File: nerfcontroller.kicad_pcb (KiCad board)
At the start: 2 copper layers, 59.7 x 48.3 mm, 40 parts, among them J1 Conn_01x02_Pin, J10 Conn_01x03_Pin, J11 Conn_01x03_Pin, J12 Conn_01x03_Pin, J13 Conn_01x03_Pin, J14 Conn_01x03_Pin, J15 Conn_01x02_Pin, J16 Conn_01x02_Pin, J17 Conn_01x03_Pin, J2 Conn_01x02_Pin, J3 Conn_01x02_Pin, J4 Conn_01x02_Pin, J5 Conn_01x03_Pin, J6 Conn_01x03_Pin, J7 Conn_01x03_Pin, J8 Conn_01x03_Pin, J9 Conn_01x03_Pin, Q1 IRL530, Q2 IRL530, Q3 IRL530, Q4 IRL530, U1 LM7805_TO220

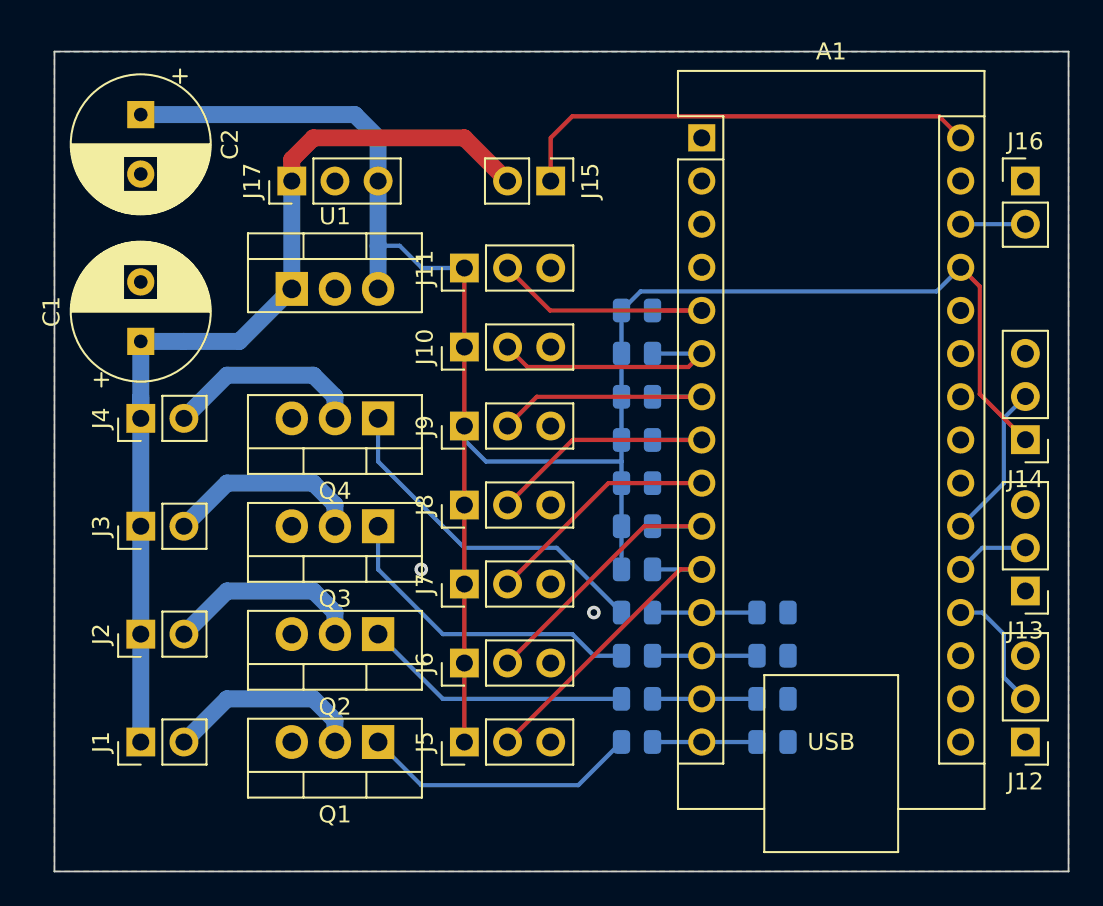
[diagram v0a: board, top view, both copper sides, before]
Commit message: added resistor values for mosfets
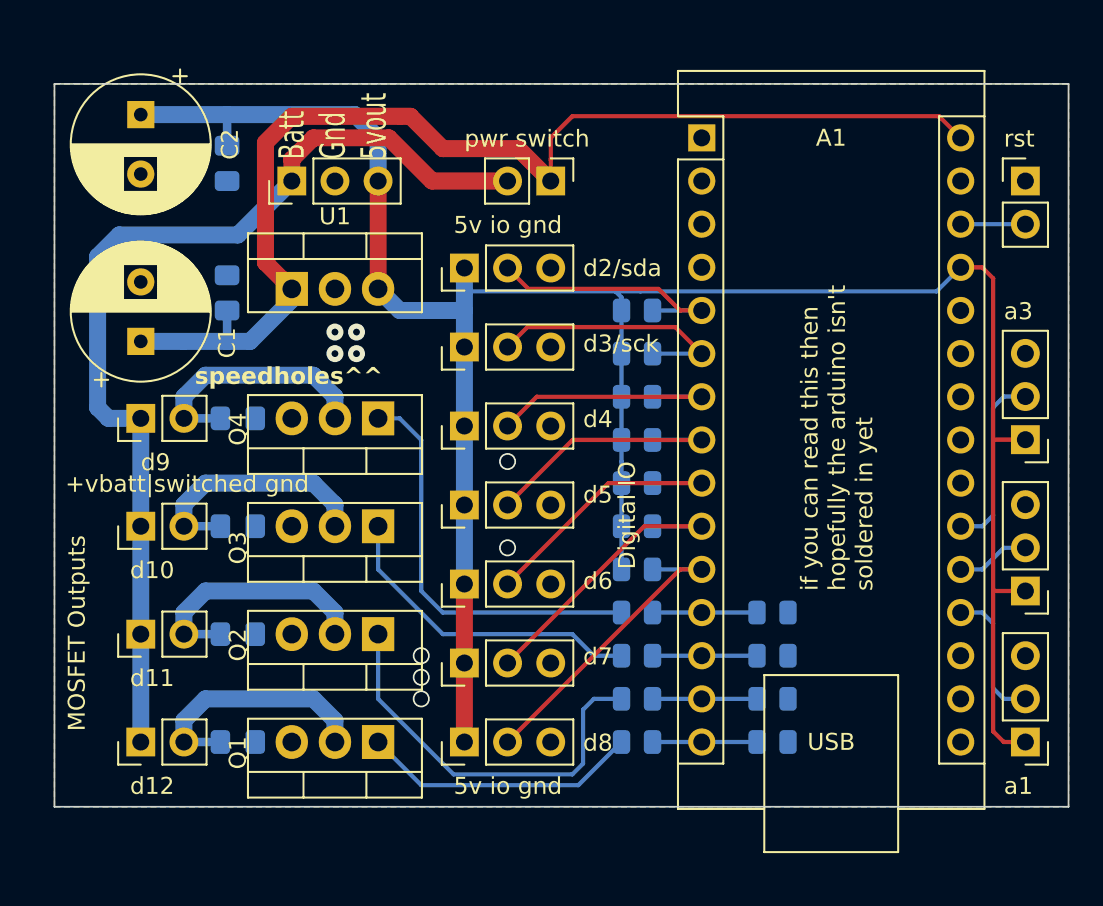
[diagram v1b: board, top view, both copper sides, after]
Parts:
- added C3: C, Capacitor_SMD:C_0805_2012Metric_Pad1.18x1.45mm_HandSolder, B.Cu at (85.1, 105.6)
- added C4: C, Capacitor_SMD:C_0805_2012Metric_Pad1.18x1.45mm_HandSolder, B.Cu at (85.1, 98.0)
- added D1: D, Diode_SMD:D_0805_2012Metric_Pad1.15x1.40mm_HandSolder, B.Cu at (85.7, 113.0)
- added D2: D, Diode_SMD:D_0805_2012Metric_Pad1.15x1.40mm_HandSolder, B.Cu at (85.7, 119.4)
- added D3: D, Diode_SMD:D_0805_2012Metric_Pad1.15x1.40mm_HandSolder, B.Cu at (85.7, 125.7)
- added D4: D, Diode_SMD:D_0805_2012Metric_Pad1.15x1.40mm_HandSolder, B.Cu at (85.7, 132.1)
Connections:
- A1 pad 30: Net-(A1-VIN) -> /12v switched
- C1 pad 1: +12V -> /12v switched
- J15 pad 1: Net-(A1-VIN) -> /12v switched
- U1 pad 1: +12V -> /12v switched
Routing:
- net /12v switched: track 0.00 -> 68.3 mm
- net Net-(A1-VIN): track 27.7 -> 0.00 mm
- net +5V: track 115.5 -> 141.4 mm
- net Net-(Q2-Pad1): track 15.9 -> 23.7 mm
- net Net-(Q4-Pad1): track 20.5 -> 24.3 mm
- net /mosfet1: track 11.7 -> 14.6 mm
- net /mosfet2: track 11.7 -> 14.6 mm
- net /mosfet4: track 11.7 -> 14.6 mm
- net /mosfet3: track 11.7 -> 14.6 mm
- net +12V: track 56.9 -> 59.6 mm
- net /a2: track 9.21 -> 10.7 mm
- net /a0: track 7.40 -> 8.15 mm
- net GND: vias 2 -> 9
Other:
- board size 59.7 x 48.3 mm -> 59.7 x 42.5 mm
- board text added: "+vbatt|switched gnd"
- board text added: "5v io gnd"
- board text added: "Batt Gnd 5vout"
- board text added: "Digital IO"
- board text added: "MOSFET Outputs"
- board text added: "a1"
- board text added: "a3"
- board text added: "d10"
- board text added: "d11"
- board text added: "d12"
- board text added: "d2/sda"
- board text added: "d3/sck"
- board text added: "d4"
- board text added: "d5"
- board text added: "d6"
- board text added: "d7"
- board text added: "d8"
- board text added: "d9"
- board text added: "if you can read this then hopefully the arduino isn't soldered in yet"
- board text added: "pwr switch"
- board text added: "rst"
- board text added: "speedholes^^"
- board text added: "|-optional pullups-|"

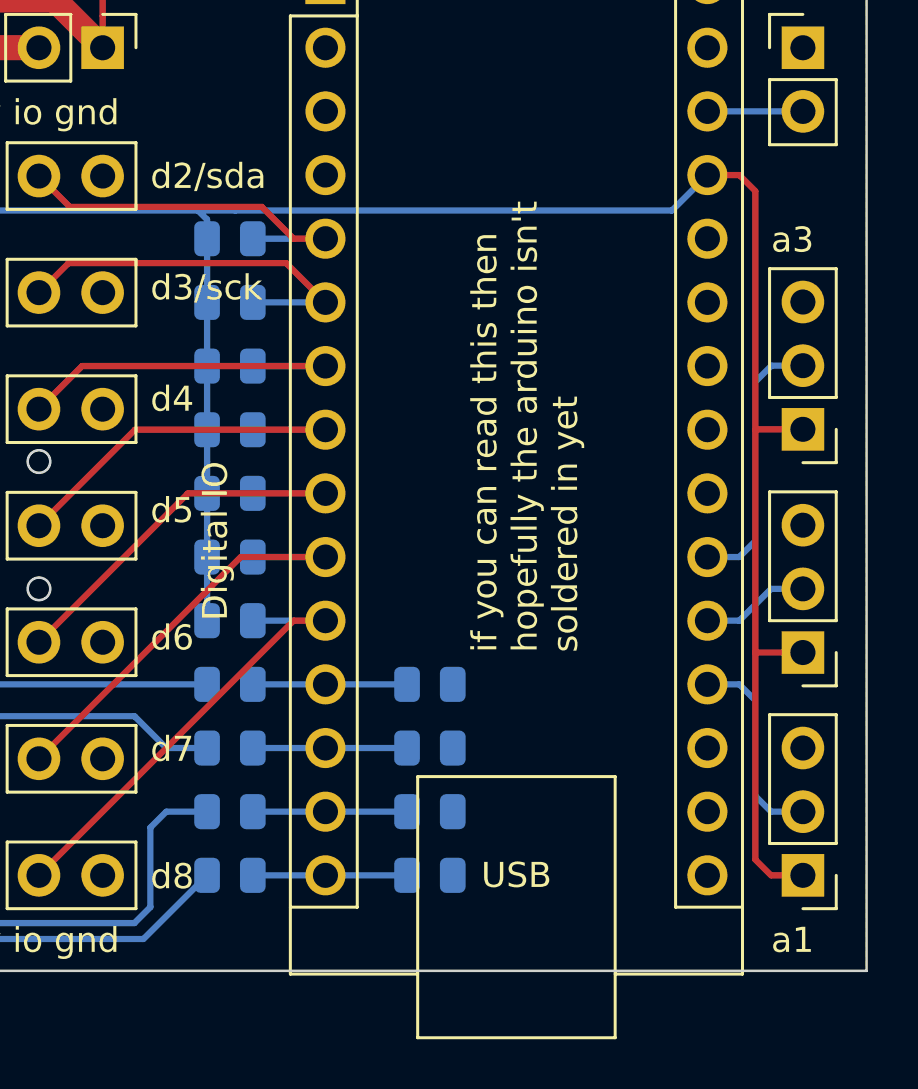
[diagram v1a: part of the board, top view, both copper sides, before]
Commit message: corrected resistor values + silkscreen goofs
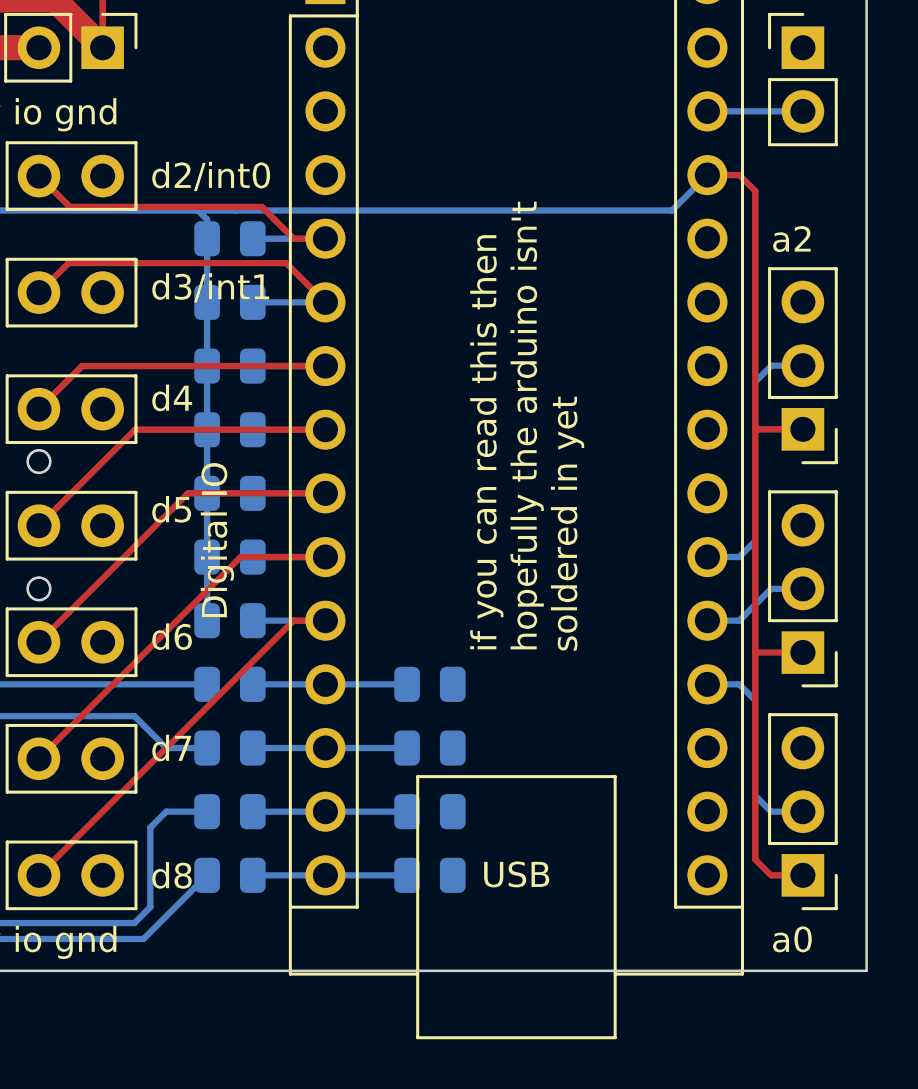
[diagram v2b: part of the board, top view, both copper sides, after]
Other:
- board text added: "a0"
- board text added: "a2"
- board text added: "d2/int0"
- board text added: "d3/int1"
- board text removed: "a1"
- board text removed: "a3"
- board text removed: "d2/sda"
- board text removed: "d3/sck"
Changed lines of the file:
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@@
     (property "ki_keywords" "cap capacitor")
     (attr smd)
-    (fp_text reference "C3" (at 0 1.68 90) (layer "B.SilkS")
+    (fp_text reference "C3" (at -0.027164 -1.677462 90) (layer "B.SilkS")
         (effects (font (size 1 1) (thickness 0.15)) (justify mirror))
     )
@@
     (effects (font (size 1.5 1) (thickness 0.15)) (justify left bottom))
   )
-  (gr_text "a1" (at 130.81 135.255) (layer "F.SilkS")
+  (gr_text "a0" (at 130.81 135.255) (layer "F.SilkS")
     (effects (font (size 1 1) (thickness 0.15)) (justify left bottom))
   )
@@
     (effects (font (size 1 1) (thickness 0.15)) (justify left bottom))
   )
-  (gr_text "d3/sck" (at 106.045 109.22) (layer "F.SilkS")
+  (gr_text "d3/int1" (at 106.045 109.22) (layer "F.SilkS")
     (effects (font (size 1 1) (thickness 0.15)) (justify left bottom))
   )
@@
     (effects (font (size 1 1) (thickness 0.15)) (justify left bottom))
   )
-  (gr_text "a3" (at 130.81 107.315) (layer "F.SilkS")
+  (gr_text "a2" (at 130.81 107.315) (layer "F.SilkS")
     (effects (font (size 1 1) (thickness 0.15)) (justify left bottom))
   )
@@
     (effects (font (size 1 1) (thickness 0.15)) (justify left bottom))
   )
-  (gr_text "d2/sda" (at 106.045 104.775) (layer "F.SilkS")
-    (effects (font (size 1 1) (thickness 0.15)) (justify left bottom))
-  )
+  (gr_text "d2/int0" (at 106.045 104.775) (layer "F.SilkS")
+    (effects (font (size 1 1) (thickness 0.15)) (justify left bottom))
+  )

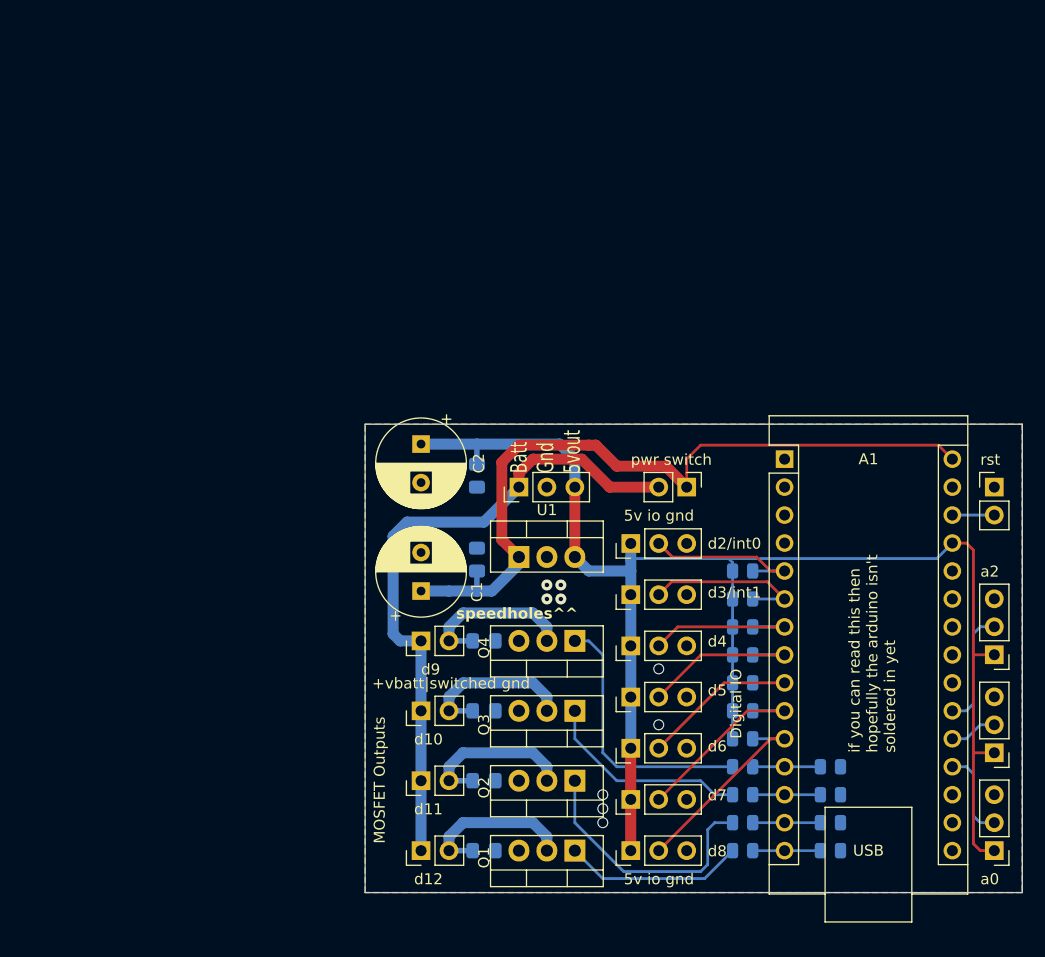
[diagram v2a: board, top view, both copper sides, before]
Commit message: added mosfet drivers and sot23 diodes
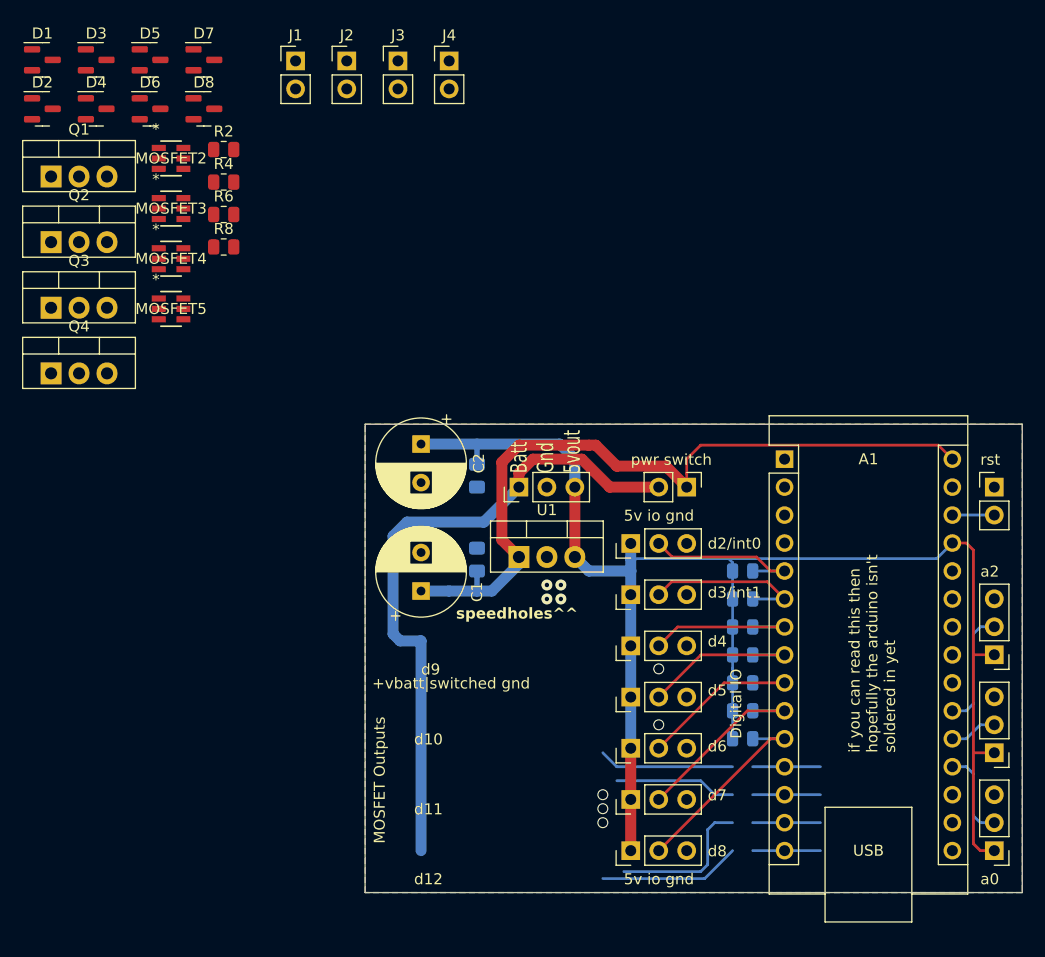
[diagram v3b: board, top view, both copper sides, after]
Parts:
- removed R1, R3, R5, R7: R, Resistor_SMD:R_0805_2012Metric
- added D5: BAV23C, Package_TO_SOT_SMD:SOT-23, F.Cu at (55.4, 60.2)
- added D6: BAV23C, Package_TO_SOT_SMD:SOT-23, F.Cu at (55.4, 64.7)
- added D7: BAV23C, Package_TO_SOT_SMD:SOT-23, F.Cu at (60.3, 60.2)
- added D8: BAV23C, Package_TO_SOT_SMD:SOT-23, F.Cu at (60.3, 64.7)
- added MOSFET2: IRS10752LTRPBF, IRS10752PBF:6L-SOT23, F.Cu at (57.3, 69.2)
- added MOSFET3: IRS10752LTRPBF, IRS10752PBF:6L-SOT23, F.Cu at (57.3, 73.8)
- added MOSFET4: IRS10752LTRPBF, IRS10752PBF:6L-SOT23, F.Cu at (57.3, 78.3)
- added MOSFET5: IRS10752LTRPBF, IRS10752PBF:6L-SOT23, F.Cu at (57.3, 82.9)
- D1, D2, D3, D4: value D -> BAV23C; footprint Diode_SMD:D_0805_2012Metric_Pad1.15x1.40mm_HandSolder -> Package_TO_SOT_SMD:SOT-23; moved to F.Cu
- R2, R4, R6, R8: value R -> 4R7; moved to F.Cu
- moved R2 84.2 mm to (62.1, 68.4)
- moved R4 78.3 mm to (62.1, 71.3)
- moved Q1 77.5 mm to (46.4, 70.8), turned to 0 degrees
- moved D4 76.0 mm to (50.5, 64.7)
- moved D3 74.4 mm to (50.5, 60.2)
- moved J1 72.6 mm to (68.6, 60.3), turned to 0 degrees
- moved R6 72.6 mm to (62.1, 74.3)
- moved Q2 68.2 mm to (46.4, 76.8), turned to 0 degrees
- moved D2 67.8 mm to (45.6, 64.7)
- moved R8 66.7 mm to (62.1, 77.2)
- moved D1 66.3 mm to (45.6, 60.2)
- moved J2 65.7 mm to (73.3, 60.3), turned to 0 degrees
- moved Q3 60.0 mm to (46.4, 82.8), turned to 0 degrees
- moved J3 59.1 mm to (77.9, 60.3), turned to 0 degrees
- moved Q4 53.4 mm to (46.4, 88.7), turned to 0 degrees
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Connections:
- net /d2 renamed Net-(A1-D2)
- net Net-(A1-D4) renamed /d4
- net Net-(A1-D6) renamed /d6
- A1 pad 12: Net-(A1-D9) -> /mosfets + drivers/D9 in
- A1 pad 13: Net-(A1-D10) -> /mosfets + drivers/D10 in
- A1 pad 14: Net-(A1-D11) -> /mosfets + drivers/D11 in
- A1 pad 15: Net-(A1-D12) -> /mosfets + drivers/D12 in
- D1 pad 1: /mosfet4 -> GND
- D2 pad 1: /mosfet3 -> +5V
- D2 pad 2: GND -> +5V
- D3 pad 1: /mosfet2 -> GND
- D4 pad 1: /mosfet1 -> +5V
- D4 pad 2: GND -> +5V
- J1 pad 1: +12V -> GND
- J1 pad 2: /mosfet1 -> /mosfet4
- J2 pad 1: +12V -> GND
- J2 pad 2: /mosfet2 -> /mosfet3
- J3 pad 2: /mosfet3 -> /mosfet2
- J4 pad 2: /mosfet4 -> /mosfet1
- Q1 pad 2: /mosfet1 -> /mosfet2
- Q2 pad 2: /mosfet2 -> /mosfet3
- Q3 pad 2: /mosfet3 -> /mosfet4
- Q4 pad 2: /mosfet4 -> /mosfet1
- R2 pad 1: Net-(A1-D12) -> Net-(Q1-Pad1)
- R2 pad 2: GND -> Net-(MOSFET3-HO)
- R4 pad 1: Net-(A1-D10) -> Net-(Q2-Pad1)
- R4 pad 2: GND -> Net-(MOSFET4-HO)
- R6 pad 1: Net-(Q2-Pad1) -> Net-(Q3-Pad1)
- R6 pad 2: Net-(A1-D11) -> Net-(MOSFET5-HO)
- R8 pad 2: Net-(A1-D9) -> Net-(MOSFET2-HO)
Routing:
- net /mosfet1: track 14.6 -> 0.00 mm
- net /mosfet2: track 14.6 -> 0.00 mm
- net /mosfet4: track 14.6 -> 0.00 mm
- net /mosfet3: track 14.6 -> 0.00 mm
- net Net-(Q4-Pad1): track 24.3 -> 12.3 mm
- net Net-(Q2-Pad1): track 23.7 -> 13.6 mm
- net Net-(Q3-Pad1): track 19.0 -> 11.0 mm
- net Net-(A1-D9): track 6.15 -> 0.00 mm
- net Net-(A1-D12): track 6.15 -> 0.00 mm
- net Net-(A1-D11): track 6.15 -> 0.00 mm
- net Net-(A1-D10): track 6.15 -> 0.00 mm
- net /mosfets + drivers/D9 in: track 0.00 -> 6.15 mm
- net /mosfets + drivers/D12 in: track 0.00 -> 6.15 mm
- net /mosfets + drivers/D11 in: track 0.00 -> 6.15 mm
- net /mosfets + drivers/D10 in: track 0.00 -> 6.15 mm
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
